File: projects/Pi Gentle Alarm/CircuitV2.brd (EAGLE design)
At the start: 85.1 x 57.2 mm, 5 parts, among them X1 RASPI_BOARD_B+_E4, X2 22-23-2021

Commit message: Added template to board
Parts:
- X1: value RASPI_BOARD_B+_E4 -> RASPI_BOARD_B+_E3; device raspberrypi_bastelstube_v13:RASPI_BOARD_B+_EDGES_4DRILL -> raspberrypi_bastelstube_v13:RASPI_BOARD_B+_EDGES_3DRILL
- moved X2 41.1 mm to (10.0, 43.0)
- moved LED1 8.89 mm to (31.0, 45.0)
- moved LED2 8.24 mm to (42.0, 41.0), turned to 90 degrees
- moved Q1 7.21 mm to (19.0, 44.0), turned to 270 degrees
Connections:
- net 5V0 renamed N$2
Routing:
- net VCC: track 15.5 -> 0.00 mm
- net GPIO17: track 13.8 -> 0.00 mm
- net N$6: track 8.20 -> 0.00 mm
- net N$1: track 6.35 -> 0.00 mm
- added copper zone on layer 1, net GND
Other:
- board size 85.1 x 57.2 mm -> 65 x 56 mm
- board text added: "BOTTOM"
- board text added: "TOP"

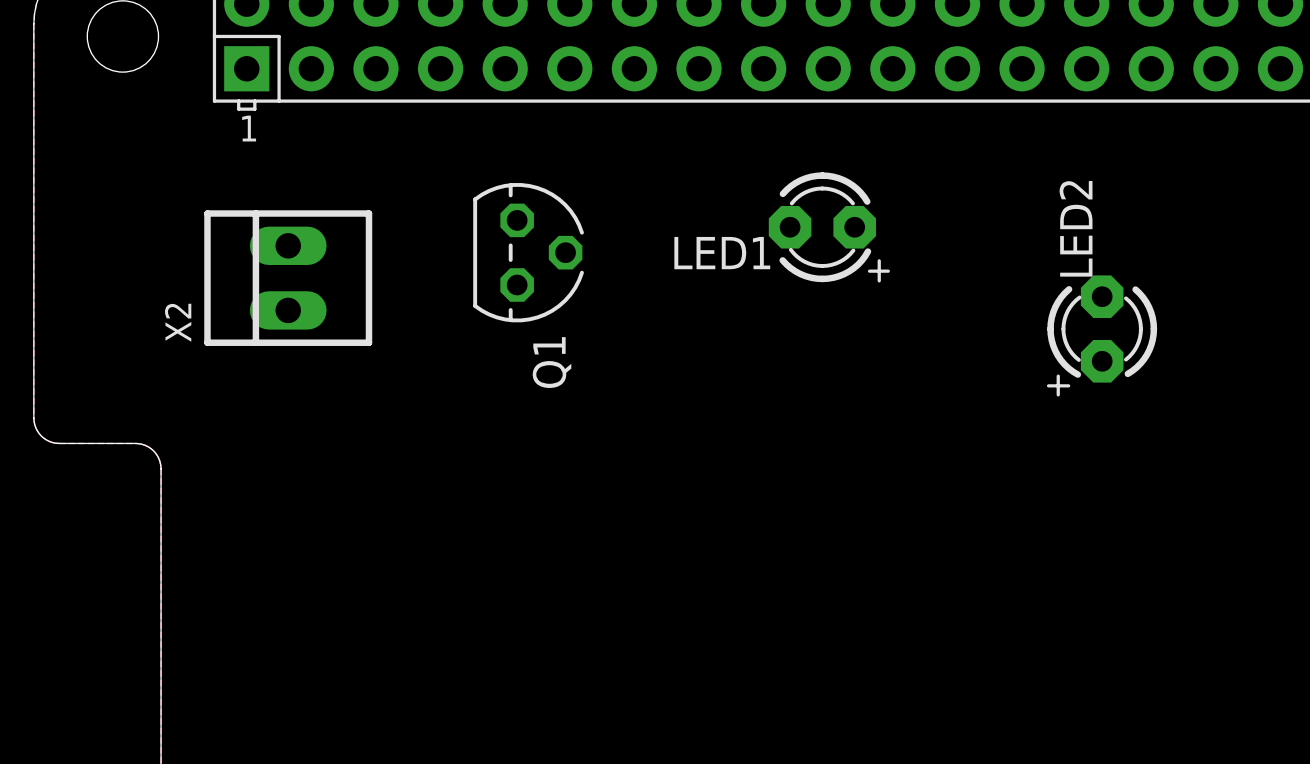
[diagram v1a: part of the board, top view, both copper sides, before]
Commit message: Changed two LED to one Large ONe
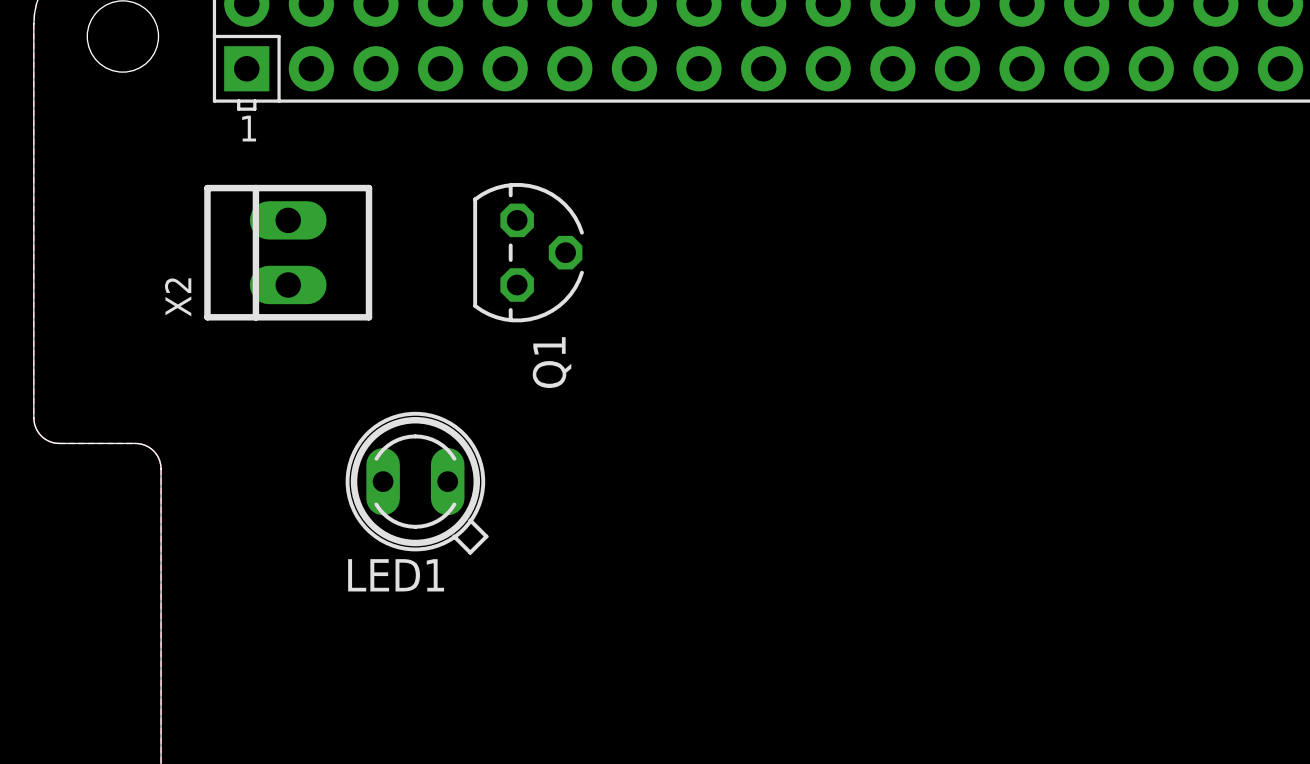
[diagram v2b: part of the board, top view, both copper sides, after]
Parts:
- removed LED2: (no value), adafruit:LED3MM
- LED1: device adafruit:LED3MM -> adafruit:SFH482
- moved LED1 18.9 mm to (15.0, 35.0)
- moved X2 1.00 mm to (10.0, 44.0)
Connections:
- removed net N$1: LED1.A, LED2.K
- net N$6: now also LED1.A; no longer LED1.K
- net VCC: now also LED1.K; no longer LED2.A
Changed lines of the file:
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@@
 <elements>
 <element name="X1" library="raspberrypi_bastelstube_v13" package="RASPI_BOARD_B+_EDGES_3DRILL" value="RASPI_BOARD_B+_E3" x="0" y="0" smashed="yes"/>
-<element name="X2" library="con-molex" library_urn="urn:adsk.eagle:library:165" package="22-23-2021" package3d_urn="urn:adsk.eagle:package:8078633/1" value="22-23-2021" x="10" y="43" smashed="yes" rot="R90">
-<attribute name="MF" value="MOLEX" x="-2" y="35" size="1.778" layer="27" rot="R90" display="off"/>
-<attribute name="MPN" value="22-23-2021" x="-2" y="35" size="1.778" layer="27" rot="R90" display="off"/>
-<attribute name="NAME" x="6.19" y="40.46" size="1.016" layer="25" ratio="10" rot="R90"/>
-<attribute name="OC_FARNELL" value="1462926" x="-2" y="35" size="1.778" layer="27" rot="R90" display="off"/>
-<attribute name="OC_NEWARK" value="25C3832" x="-2" y="35" size="1.778" layer="27" rot="R90" display="off"/>
-<attribute name="POPULARITY" value="40" x="-2" y="35" size="1.778" layer="27" rot="R90" display="off"/>
-<attribute name="VALUE" x="15.08" y="40.46" size="1.016" layer="27" ratio="10" rot="R90"/>
+<element name="X2" library="con-molex" library_urn="urn:adsk.eagle:library:165" package="22-23-2021" package3d_urn="urn:adsk.eagle:package:8078633/1" value="22-23-2021" x="10" y="44" smashed="yes" rot="R90">
+<attribute name="MF" value="MOLEX" x="-2" y="36" size="1.778" layer="27" rot="R90" display="off"/>
+<attribute name="MPN" value="22-23-2021" x="-2" y="36" size="1.778" layer="27" rot="R90" display="off"/>
+<attribute name="NAME" x="6.19" y="41.46" size="1.016" layer="25" ratio="10" rot="R90"/>
+<attribute name="OC_FARNELL" value="1462926" x="-2" y="36" size="1.778" layer="27" rot="R90" display="off"/>
+<attribute name="OC_NEWARK" value="25C3832" x="-2" y="36" size="1.778" layer="27" rot="R90" display="off"/>
+<attribute name="POPULARITY" value="40" x="-2" y="36" size="1.778" layer="27" rot="R90" display="off"/>
+<attribute name="VALUE" x="15.08" y="41.46" size="1.016" layer="27" ratio="10" rot="R90"/>
 </element>
 <element name="Q1" library="transistors" package="TO-92" value="" x="19" y="44" smashed="yes" rot="R270">
@@
 <attribute name="VALUE" x="17.73" y="40.825" size="1.27" layer="27" ratio="10" rot="R270"/>
 </element>
-<element name="LED1" library="adafruit" library_urn="urn:adsk.eagle:library:420" package="LED3MM" package3d_urn="urn:adsk.eagle:package:6240537/1" value="" x="31" y="45" smashed="yes" rot="R180">
-<attribute name="NAME" x="29.095" y="44.619" size="1.27" layer="25" ratio="10" rot="R180"/>
-<attribute name="VALUE" x="29.095" y="46.651" size="1.27" layer="27" ratio="10" rot="R180"/>
-</element>
-<element name="LED2" library="adafruit" library_urn="urn:adsk.eagle:library:420" package="LED3MM" package3d_urn="urn:adsk.eagle:package:6240537/1" value="" x="42" y="41" smashed="yes" rot="R90">
-<attribute name="NAME" x="41.619" y="42.905" size="1.27" layer="25" ratio="10" rot="R90"/>
-<attribute name="VALUE" x="43.651" y="42.905" size="1.27" layer="27" ratio="10" rot="R90"/>
+<element name="LED1" library="adafruit" library_urn="urn:adsk.eagle:library:420" package="SFH482" package3d_urn="urn:adsk.eagle:package:6240546/1" value="" x="15" y="35" smashed="yes" rot="R180">
+<attribute name="NAME" x="16.27" y="31.952" size="1.27" layer="25" ratio="10" rot="R180"/>
+<attribute name="VALUE" x="16.27" y="39.318" size="1.27" layer="27" ratio="10" rot="R180"/>
 </element>
 </elements>
@@
 <signal name="VCC">
 <contactref element="X2" pad="1"/>
-<contactref element="LED2" pad="A"/>
-<wire x1="10" y1="41.73" x2="42" y2="39.73" width="0" layer="19" extent="1-1"/>
+<contactref element="LED1" pad="K"/>
+<wire x1="13.73" y1="35" x2="10" y2="42.73" width="0" layer="19" extent="1-1"/>
 </signal>
 <signal name="GPIO17">
@@
 <signal name="N$6">
 <contactref element="Q1" pad="3"/>
-<contactref element="LED1" pad="K"/>
-<wire x1="19" y1="42.73" x2="29.73" y2="45" width="0" layer="19" extent="1-1"/>
-</signal>
-<signal name="N$1">
 <contactref element="LED1" pad="A"/>
-<contactref element="LED2" pad="K"/>
-<wire x1="32.27" y1="45" x2="42" y2="42.27" width="0" layer="19" extent="1-1"/>
+<wire x1="16.27" y1="35" x2="19" y2="42.73" width="0" layer="19" extent="1-1"/>
 </signal>
 <signal name="N$2">

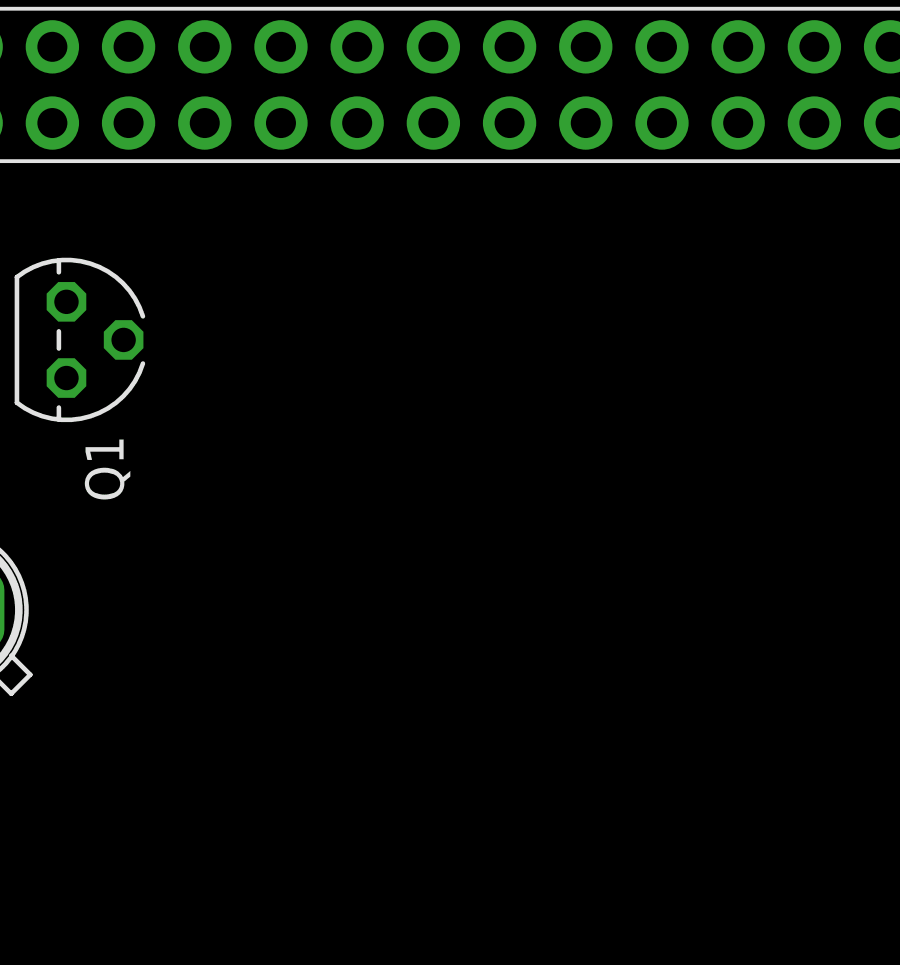
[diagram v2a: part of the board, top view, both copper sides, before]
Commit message: Finishing steps for the hat
Added a fuse to protect the pi
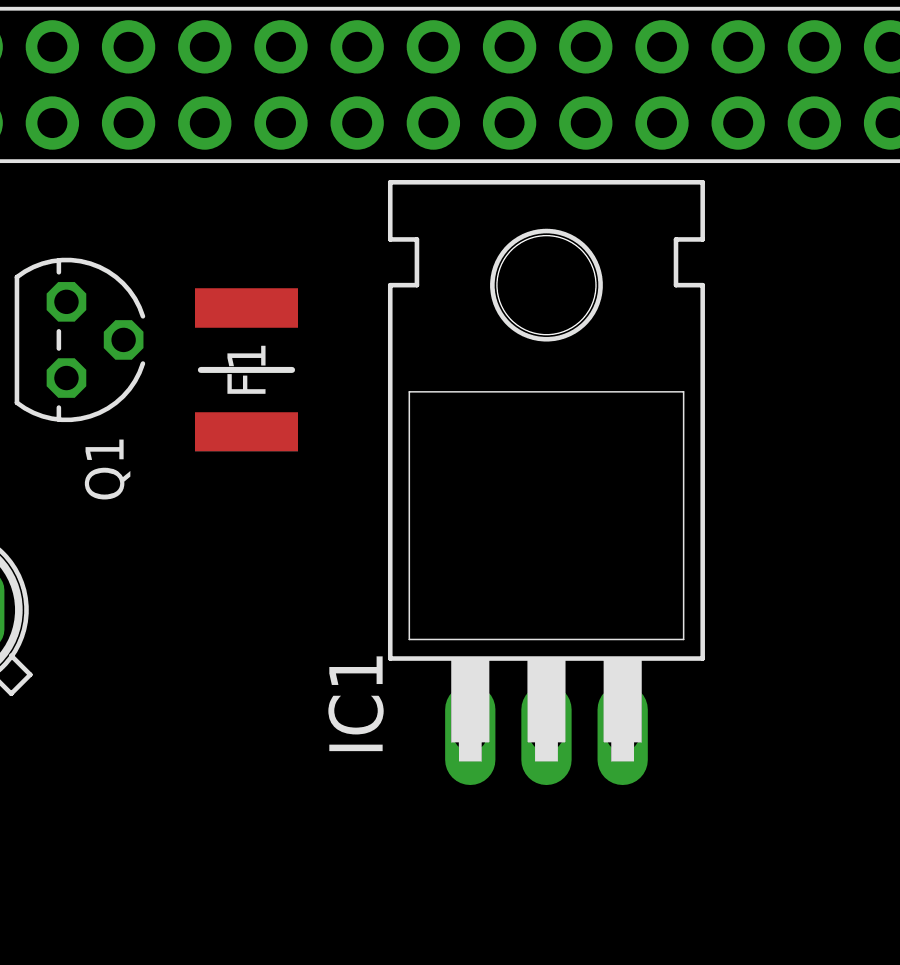
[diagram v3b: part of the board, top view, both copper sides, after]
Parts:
- added F1: MINISMDC110F-2, MINISMDC110F-2:FUSC4632X62N
- added IC1: 7805T, linear:TO220H
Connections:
- new net N$1: F1.1, X1.2
- net GND: now also IC1.2
- net N$2: now also F1.2, IC1.3; no longer X1.2
- net VCC: now also IC1.1
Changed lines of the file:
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@@
 <layer number="44" name="Drills" color="7" fill="1" visible="no" active="yes"/>
 <layer number="45" name="Holes" color="7" fill="1" visible="no" active="yes"/>
-<layer number="46" name="Milling" color="3" fill="1" visible="no" active="yes"/>
+<layer number="46" name="Milling" color="3" fill="1" visible="yes" active="yes"/>
 <layer number="47" name="Measures" color="7" fill="1" visible="no" active="yes"/>
-<layer number="48" name="Document" color="7" fill="1" visible="no" active="yes"/>
+<layer number="48" name="Document" color="16" fill="1" visible="yes" active="yes"/>
 <layer number="49" name="Reference" color="7" fill="1" visible="no" active="yes"/>
 <layer number="50" name="dxf" color="7" fill="1" visible="no" active="no"/>
@@
 <attribute name="VALUE" x="16.27" y="39.318" size="1.27" layer="27" ratio="10" rot="R180"/>
 </element>
+<element name="IC1" library="linear" library_urn="urn:adsk.eagle:library:262" package="TO220H" package3d_urn="urn:adsk.eagle:package:16414/1" value="7805T" x="35" y="41" smashed="yes">
+<attribute name="NAME" x="29.539" y="30.078" size="1.778" layer="25" ratio="10" rot="R90"/>
+<attribute name="POPULARITY" value="35" x="35" y="41" size="1.778" layer="27" display="off"/>
+<attribute name="VALUE" x="42.366" y="29.951" size="1.778" layer="27" ratio="10" rot="R90"/>
+</element>
+<element name="F1" library="MINISMDC110F-2" package="FUSC4632X62N" value="MINISMDC110F-2" x="25" y="43" smashed="yes" rot="R270">
+<attribute name="DESCRIPTION" value="Littelfuse 1.1A Surface Mount Resettable Fuse, 8V dc" x="25" y="43" size="1.778" layer="27" rot="R270" display="off"/>
+<attribute name="HEIGHT" value="0.62mm" x="25" y="43" size="1.778" layer="27" rot="R270" display="off"/>
+<attribute name="MANUFACTURER_NAME" value="LITTELFUSE" x="25" y="43" size="1.778" layer="27" rot="R270" display="off"/>
+<attribute name="MANUFACTURER_PART_NUMBER" value="MINISMDC110F-2" x="25" y="43" size="1.778" layer="27" rot="R270" display="off"/>
+<attribute name="MOUSER_PART_NUMBER" value="650-MINISMDC110F-2" x="25" y="43" size="1.778" layer="27" rot="R270" display="off"/>
+<attribute name="MOUSER_PRICE-STOCK" value="https://www.mouser.com/Search/Refine.aspx?Keyword=650-MINISMDC110F-2" x="25" y="43" size="1.778" layer="27" rot="R270" display="off"/>
+<attribute name="NAME" x="25" y="43" size="1.27" layer="25" rot="R270" align="center"/>
+<attribute name="VALUE" x="25" y="43" size="1.27" layer="27" rot="R270" align="center"/>
+</element>
 </elements>
 <signals>
@@
 <contactref element="X2" pad="2"/>
 <contactref element="Q1" pad="1"/>
+<contactref element="IC1" pad="2"/>
 </signal>
 <signal name="3V3">
@@
 <contactref element="X2" pad="1"/>
 <contactref element="LED1" pad="K"/>
-<wire x1="13.73" y1="35" x2="10" y2="42.73" width="0" layer="19" extent="1-1"/>
+<contactref element="IC1" pad="1"/>
+<wire x1="13.73" y1="35" x2="32.46" y2="30.84" width="0" layer="19" extent="1-1"/>
+<wire x1="10" y1="42.73" x2="13.73" y2="35" width="0" layer="19" extent="1-1"/>
 </signal>
 <signal name="GPIO17">
@@
 <wire x1="16.27" y1="35" x2="19" y2="42.73" width="0" layer="19" extent="1-1"/>
 </signal>
+<signal name="N$1">
+<contactref element="X1" pad="2"/>
+<contactref element="F1" pad="1"/>
+<wire x1="8.37" y1="53.77" x2="25" y2="45.065" width="0" layer="19" extent="1-1"/>
+</signal>
 <signal name="N$2">
-<contactref element="X1" pad="2"/>
+<contactref element="IC1" pad="3"/>
+<contactref element="F1" pad="2"/>
+<wire x1="25" y1="40.935" x2="37.54" y2="30.84" width="0" layer="19" extent="1-1"/>
 </signal>
 </signals>
